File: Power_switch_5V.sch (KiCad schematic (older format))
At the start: 5 parts

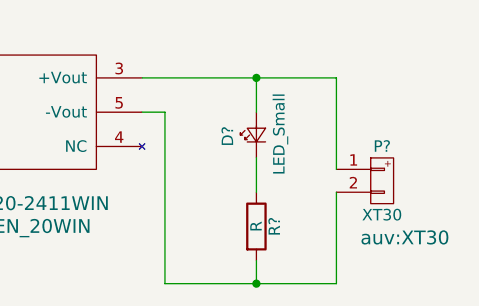
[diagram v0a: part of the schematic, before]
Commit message: change xt30 to xt60 in Power_switch_5V.sch
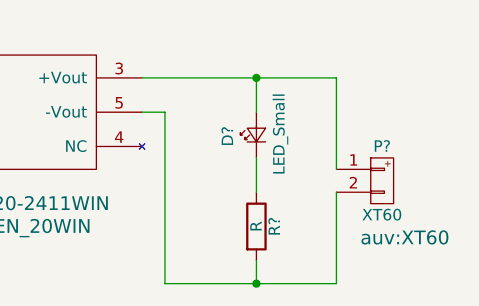
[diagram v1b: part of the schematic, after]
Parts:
- removed P?: XT30, auv:XT30, symbol XT30
- added P?: XT60, auv:XT60, symbol XT60
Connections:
- net at D?.2 (A), U?.3 (+Vout): now also P?.1 (P1)
- net at R?.2, U?.5 (-Vout): now also P?.2 (P2)
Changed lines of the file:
@@
-	1    0    0    -1
-$EndComp
-$Comp
-L XT30 P?
-U 1 1 58C992B6
-P 7150 3600
-F 0 "P?" H 7150 3750 50  0000 C CNN
-F 1 "XT30" H 7150 3450 50  0000 C CNN
-F 2 "auv:XT30" H 7250 3350 60  0000 C CNN
-F 3 "" H 7150 3600 60  0000 C CNN
-	1    7150 3600
 	1    0    0    -1
 $EndComp
@@
 Wire Wire Line
 	3800 3150 5000 3150
+$Comp
+L XT60 P?
+U 1 1 58C9F835
+P 7150 3600
+F 0 "P?" H 7150 3750 50  0000 C CNN
+F 1 "XT60" H 7150 3450 50  0000 C CNN
+F 2 "auv:XT60" H 7250 3350 60  0000 C CNN
+F 3 "" H 7150 3600 60  0000 C CNN
+	1    7150 3600
+	1    0    0    -1
+$EndComp
 $EndSCHEMATC

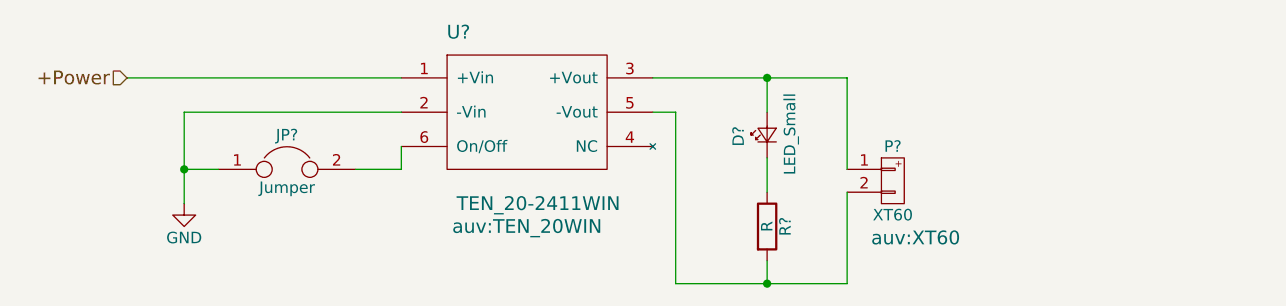
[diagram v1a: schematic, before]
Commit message: power_switch_5v have three xt60 connector at output port
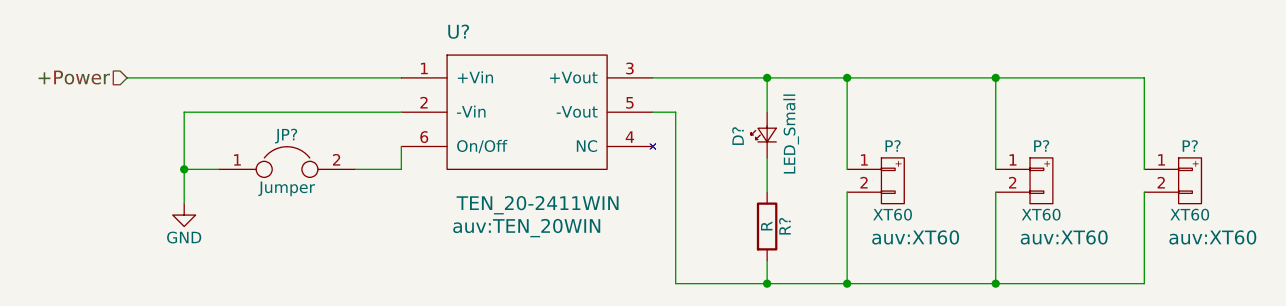
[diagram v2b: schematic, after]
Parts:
- added P? (x2): XT60, auv:XT60, symbol XT60
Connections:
- net at D?.2 (A), P?.1 (P1), U?.3 (+Vout): now also P?.1 (P1), P?.1 (P1)
- net at P?.2 (P2), R?.2, U?.5 (-Vout): now also P?.2 (P2), P?.2 (P2)
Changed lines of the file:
@@
 Connection ~ 4050 3550
 Wire Wire Line
-	6100 3150 6950 3150
+	6100 3150 8250 3150
 Wire Wire Line
 	6600 3150 6600 3300
@@
 	6200 3300 6200 4050
 Wire Wire Line
-	6200 4050 6950 4050
+	6200 4050 8250 4050
 Wire Wire Line
 	6600 4050 6600 3950
@@
 	1    0    0    -1
 $EndComp
+$Comp
+L XT60 P?
+U 1 1 58DFD635
+P 7800 3600
+F 0 "P?" H 7800 3750 50  0000 C CNN
+F 1 "XT60" H 7800 3450 50  0000 C CNN
+F 2 "auv:XT60" H 7900 3350 60  0000 C CNN
+F 3 "" H 7800 3600 60  0000 C CNN
+	1    7800 3600
+	1    0    0    -1
+$EndComp
+Connection ~ 6950 3150
+Connection ~ 6950 4050
+$Comp
+L XT60 P?
+U 1 1 58DFD6BF
+P 8450 3600
+F 0 "P?" H 8450 3750 50  0000 C CNN
+F 1 "XT60" H 8450 3450 50  0000 C CNN
+F 2 "auv:XT60" H 8550 3350 60  0000 C CNN
+F 3 "" H 8450 3600 60  0000 C CNN
+	1    8450 3600
+	1    0    0    -1
+$EndComp
+Wire Wire Line
+	8250 3150 8250 3550
+Wire Wire Line
+	8250 4050 8250 3650
+Wire Wire Line
+	7600 3550 7600 3150
+Connection ~ 7600 3150
+Wire Wire Line
+	7600 3650 7600 4050
+Connection ~ 7600 4050
 $EndSCHEMATC
